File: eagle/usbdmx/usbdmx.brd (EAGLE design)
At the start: 63.2 x 50.2 mm, 34 parts, among them IC1 MAX3468CSA, IC2 MAX3468CSA, Q1 16MHz

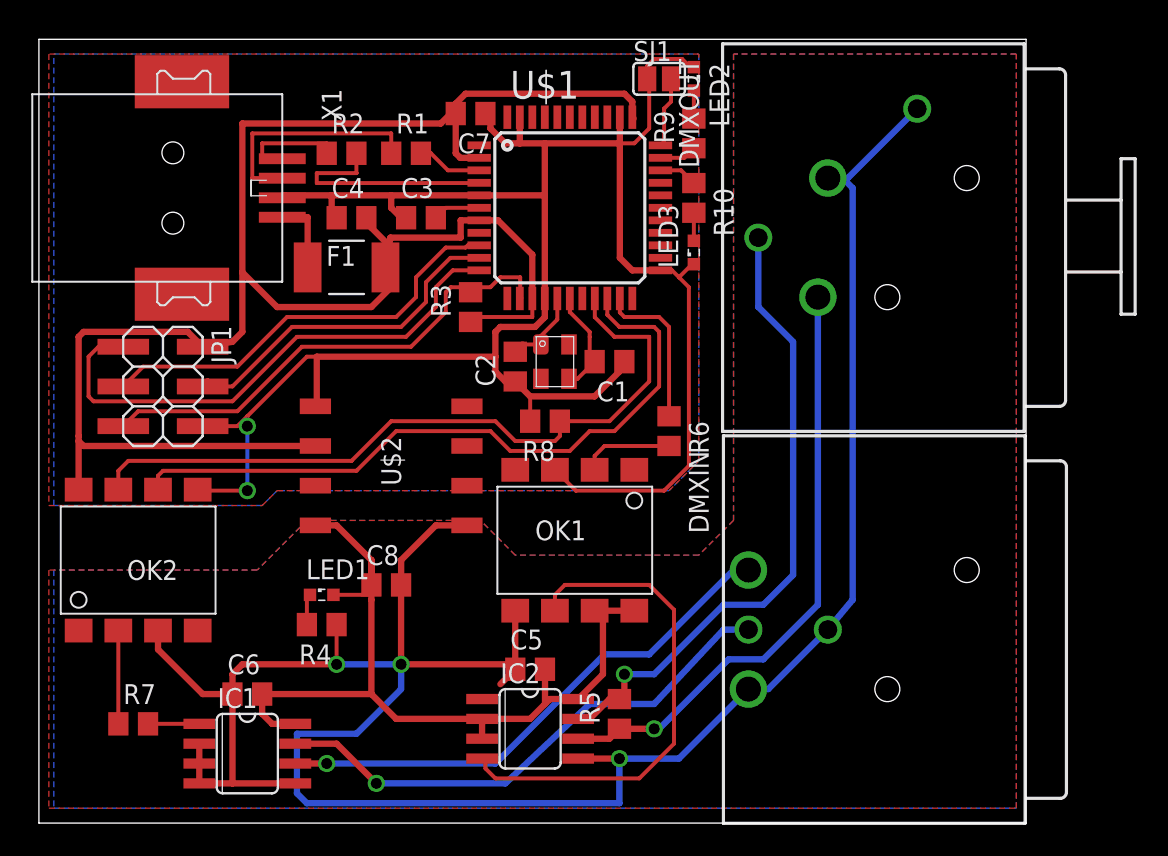
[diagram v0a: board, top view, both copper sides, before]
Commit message: make design smaller since the neutriks can be put closer
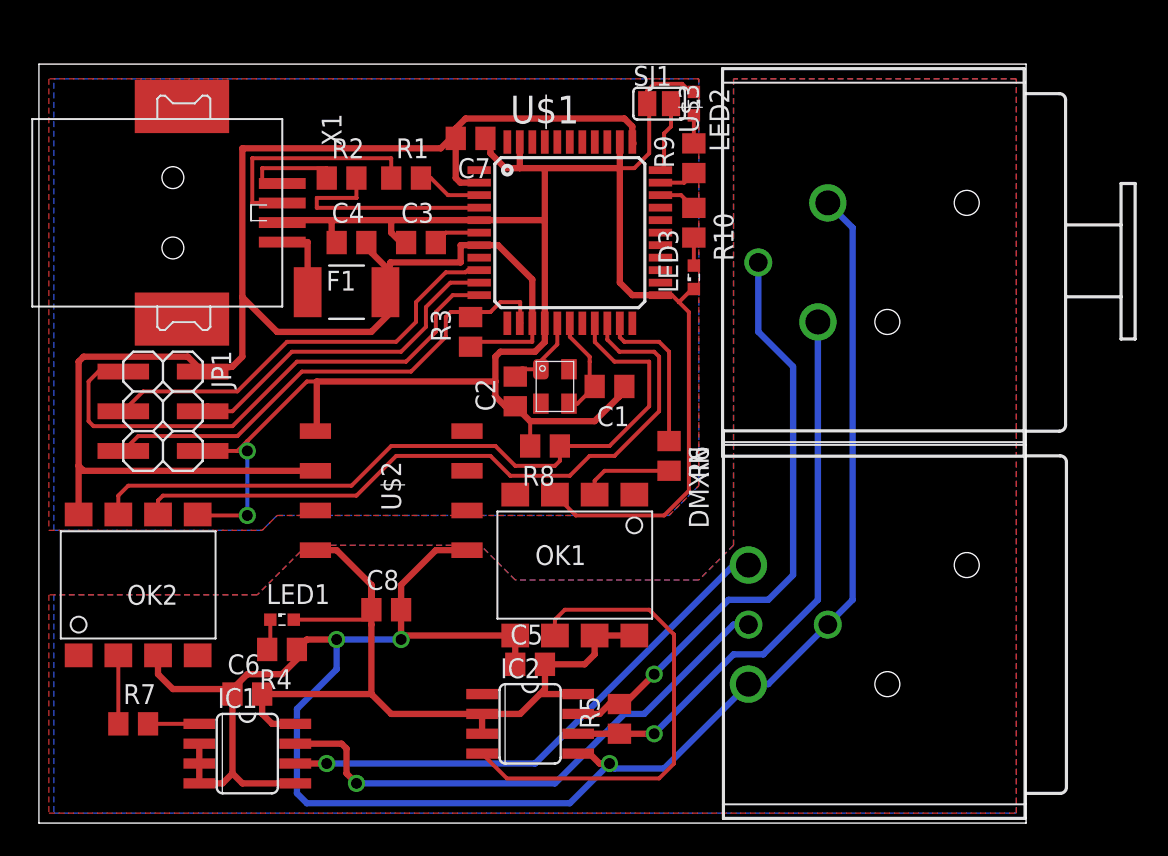
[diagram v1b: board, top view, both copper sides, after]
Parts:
- removed DMXOUT: NC3FAH2, con-neutrik_ag:NC3FAH2
- added U$3: NC3SANSFAH1, con-neutrik_ag:NC3FAH1
- DMXIN: value NC3MBH -> NC3MBH-B; device con-neutrik_ag:NC3MBH -> con-neutrik_ag:NC3MBH-B
- moved LED1 3.00 mm to (15.6, 13.0)
- moved R4 3.00 mm to (15.6, 11.1)
- moved C7 1.59 mm to (27.6, 43.8)
- moved F1 1.59 mm to (19.7, 34.0)
- moved LED3 1.59 mm to (41.9, 34.9)
- moved R10 1.59 mm to (41.9, 38.4)
- moved C2 1.59 mm to (30.5, 27.6)
- moved JP1 1.59 mm to (9.21, 27.6)
- moved R3 1.59 mm to (27.6, 31.4)
- moved R8 1.59 mm to (32.4, 24.1)
- moved C8 1.59 mm to (22.2, 13.7)
- moved OK2 1.59 mm to (6.35, 15.2)
- moved C1 1.59 mm to (36.5, 27.9)
- moved C3 1.59 mm to (24.4, 37.1)
- moved C4 1.59 mm to (20.0, 37.1)
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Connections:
- net N$12: now also U$3.2; no longer DMXOUT.2
- net N$17: now also U$3.3; no longer DMXOUT.3
- net SGND: now also U$3.1+G; no longer DMXOUT.1, DMXOUT.G
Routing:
- net SGND: track 154.5 -> 132.0 mm
- net N$17: track 40.8 -> 38.4 mm
- net SVCC: track 56.5 -> 54.4 mm
- net N$12: track 38.6 -> 36.7 mm
- net N$23: track 5.97 -> 4.38 mm
- net N$29: track 34.1 -> 35.2 mm
- net N$20: track 32.1 -> 31.1 mm
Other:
- board size 63.2 x 50.2 mm -> 63.2 x 48.6 mm

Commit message: add a necessary pull-up
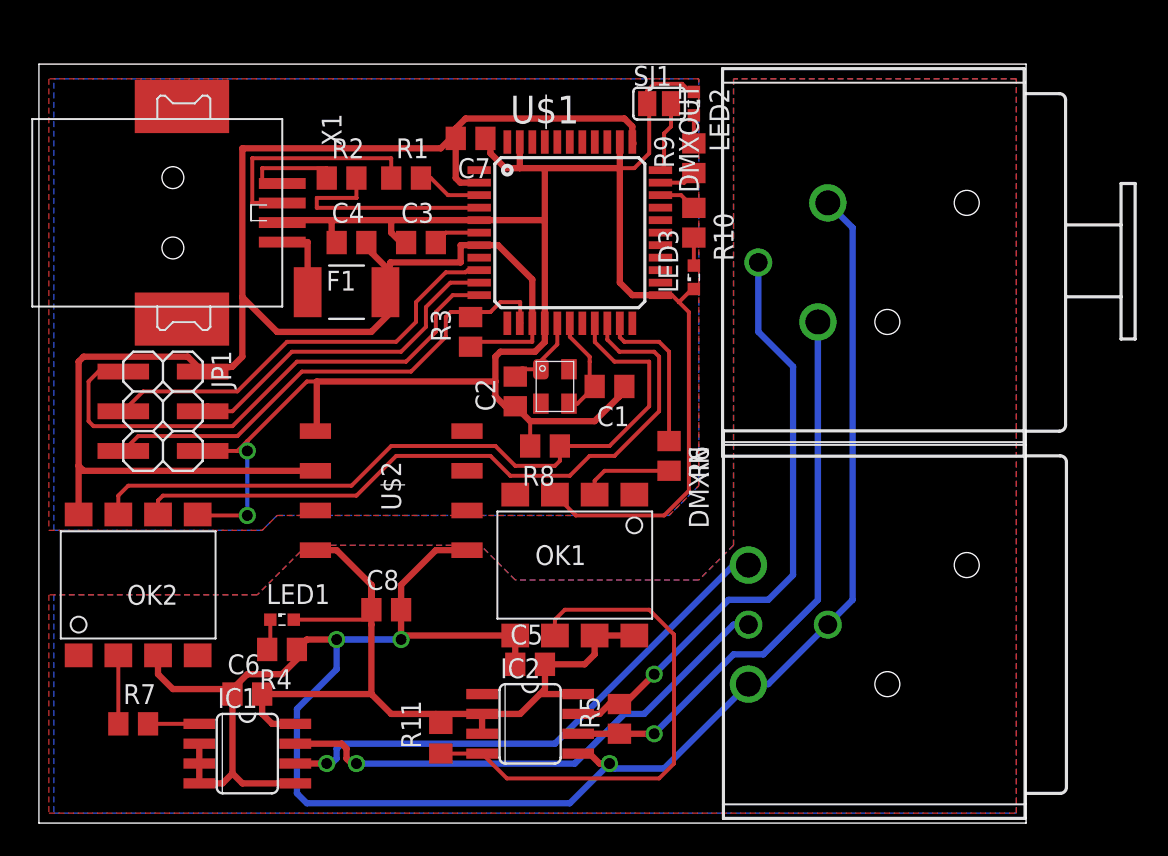
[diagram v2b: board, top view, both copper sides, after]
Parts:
- added R11: 10k, rcl:R0805
- renumbered U$3 to DMXOUT
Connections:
- net N$20: now also R11.1
- net SVCC: now also R11.2
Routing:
- net N$20: track 31.1 -> 33.8 mm
- net N$29: track 35.2 -> 33.6 mm
- net SVCC: track 54.4 -> 55.1 mm
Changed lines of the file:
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@@
 <layer number="23" name="tOrigins" color="15" fill="1" visible="yes" active="yes"/>
 <layer number="24" name="bOrigins" color="15" fill="1" visible="yes" active="yes"/>
-<layer number="25" name="tNames" color="7" fill="1" visible="yes" active="yes"/>
+<layer number="25" name="tNames" color="7" fill="1" visible="no" active="yes"/>
 <layer number="26" name="bNames" color="7" fill="1" visible="yes" active="yes"/>
-<layer number="27" name="tValues" color="7" fill="1" visible="yes" active="yes"/>
+<layer number="27" name="tValues" color="7" fill="1" visible="no" active="yes"/>
 <layer number="28" name="bValues" color="7" fill="1" visible="yes" active="yes"/>
 <layer number="29" name="tStop" color="7" fill="3" visible="no" active="yes"/>
@@
 <element name="LED3" library="led" package="SML0603" value="" x="41.91" y="34.925" rot="R90"/>
 <element name="SJ1" library="jumper" package="SJ" value="" x="39.6875" y="46.0375"/>
-<element name="U$3" library="con-neutrik_ag" package="NC3FAH1" value="NC3SANSFAH1" x="49.8475" y="35.8775" rot="R270"/>
+<element name="DMXOUT" library="con-neutrik_ag" package="NC3FAH1" value="NC3SANSFAH1" x="49.8475" y="35.8775" rot="R270"/>
+<element name="R11" library="rcl" package="R0805" value="10k" x="25.7175" y="5.3975" rot="R90"/>
 </elements>
 <signals>
@@
 <wire x1="48.26" y1="29.21" x2="46.0325" y2="31.4375" width="0.4064" layer="16"/>
 <wire x1="46.6725" y1="14.2875" x2="44.1325" y2="14.2875" width="0.4064" layer="16"/>
-<contactref element="U$3" pad="3"/>
+<contactref element="DMXOUT" pad="3"/>
 <wire x1="46.0325" y1="31.4375" x2="46.0325" y2="35.8775" width="0.4064" layer="16"/>
 <wire x1="34.5059" y1="6.985" x2="35.8775" y2="6.985" width="0.4064" layer="1"/>
@@
 <wire x1="21.2725" y1="15.24" x2="21.2725" y2="15.2425" width="0.4064" layer="1"/>
 <wire x1="21.2725" y1="15.2425" x2="21.275" y2="13.6525" width="0.4064" layer="1"/>
-<contactref element="OK1" pad="8"/>
 <contactref element="OK1" pad="7"/>
 <wire x1="28.3591" y1="6.985" x2="28.3591" y2="5.715" width="0.4064" layer="1"/>
@@
 <wire x1="16.3075" y1="13.0175" x2="21.275" y2="13.0175" width="0.254" layer="1"/>
 <wire x1="21.275" y1="13.0175" x2="21.275" y2="12.7" width="0.254" layer="1"/>
-<wire x1="38.1" y1="12.0015" x2="36.195" y2="12.0015" width="0.4064" layer="1"/>
 <wire x1="36.195" y1="12.0015" x2="35.56" y2="12.0015" width="0.4064" layer="1"/>
 <wire x1="35.875" y1="11.6865" x2="35.56" y2="12.0015" width="0.4064" layer="1"/>
@@
 <wire x1="14.2875" y1="6.985" x2="14.2875" y2="8.2525" width="0.4064" layer="1"/>
 <wire x1="14.2875" y1="8.2525" x2="14.285" y2="8.255" width="0.4064" layer="1"/>
-<wire x1="28.3591" y1="6.985" x2="22.545" y2="6.985" width="0.4064" layer="1"/>
+<wire x1="28.3591" y1="6.985" x2="25.4" y2="6.985" width="0.4064" layer="1"/>
+<wire x1="25.4" y1="6.985" x2="22.545" y2="6.985" width="0.4064" layer="1"/>
 <wire x1="22.545" y1="6.985" x2="21.275" y2="8.255" width="0.4064" layer="1"/>
+<contactref element="OK1" pad="8"/>
+<contactref element="R11" pad="2"/>
+<wire x1="25.7175" y1="6.3475" x2="25.4" y2="6.665" width="0.254" layer="1"/>
+<wire x1="25.4" y1="6.665" x2="25.4" y2="6.985" width="0.254" layer="1"/>
+<wire x1="36.195" y1="12.0015" x2="38.1" y2="12.0015" width="0.4064" layer="1"/>
 </signal>
 <signal name="SGND">
@@
 <wire x1="16.51" y1="7.3025" x2="16.51" y2="1.905" width="0.4064" layer="16"/>
 <wire x1="16.51" y1="1.905" x2="17.145" y2="1.27" width="0.4064" layer="16"/>
-<contactref element="U$3" pad="1+G"/>
+<contactref element="DMXOUT" pad="1+G"/>
 <wire x1="52.07" y1="14.2875" x2="52.07" y2="38.1" width="0.4064" layer="16"/>
 <wire x1="52.07" y1="38.1" x2="50.4825" y2="39.6875" width="0.4064" layer="16"/>
@@
 <wire x1="39.6875" y1="2.8575" x2="40.64" y2="3.81" width="0.254" layer="1"/>
 <wire x1="40.64" y1="3.81" x2="40.64" y2="12.065" width="0.254" layer="1"/>
+<contactref element="R11" pad="1"/>
+<wire x1="28.3591" y1="4.445" x2="28.3566" y2="4.4475" width="0.254" layer="1"/>
+<wire x1="28.3566" y1="4.4475" x2="25.7175" y2="4.4475" width="0.254" layer="1"/>
 </signal>
 <signal name="N$21">
@@
 <contactref element="IC2" pad="6"/>
 <contactref element="R5" pad="1"/>
-<contactref element="U$3" pad="2"/>
+<contactref element="DMXOUT" pad="2"/>
 <wire x1="49.8475" y1="14.2875" x2="49.8475" y2="32.0675" width="0.4064" layer="16"/>
 <wire x1="34.5059" y1="5.715" x2="37.145" y2="5.715" width="0.4064" layer="1"/>
@@
 <contactref element="IC1" pad="7"/>
 <contactref element="DMXIN" pad="3"/>
-<via x="20.32" y="2.54" extent="1-16" drill="0.7" shape="square"/>
-<wire x1="20.32" y1="2.54" x2="33.02" y2="2.54" width="0.4064" layer="16"/>
+<via x="20.32" y="3.81" extent="1-16" drill="0.7" shape="square"/>
+<wire x1="20.32" y1="3.81" x2="34.29" y2="3.81" width="0.4064" layer="16"/>
 <wire x1="16.4084" y1="5.08" x2="19.3675" y2="5.08" width="0.4064" layer="1"/>
-<wire x1="19.3675" y1="5.08" x2="19.685" y2="4.7625" width="0.4064" layer="1"/>
-<wire x1="19.685" y1="4.7625" x2="19.685" y2="3.175" width="0.4064" layer="1"/>
-<wire x1="19.685" y1="3.175" x2="20.32" y2="2.54" width="0.4064" layer="1"/>
-<wire x1="33.02" y1="2.54" x2="37.465" y2="6.985" width="0.4064" layer="16"/>
+<wire x1="34.29" y1="3.81" x2="37.465" y2="6.985" width="0.4064" layer="16"/>
 <wire x1="37.465" y1="6.985" x2="38.735" y2="6.985" width="0.4064" layer="16"/>
 <wire x1="38.735" y1="6.985" x2="44.45" y2="12.7" width="0.4064" layer="16"/>
 <wire x1="44.45" y1="12.7" x2="45.4025" y2="12.7" width="0.4064" layer="16"/>
+<wire x1="19.3675" y1="5.08" x2="19.685" y2="4.7625" width="0.4064" layer="1"/>
+<wire x1="19.685" y1="4.7625" x2="19.685" y2="4.1275" width="0.4064" layer="1"/>
+<wire x1="19.685" y1="4.1275" x2="20.0025" y2="3.81" width="0.4064" layer="1"/>
+<wire x1="20.0025" y1="3.81" x2="20.32" y2="3.81" width="0.4064" layer="1"/>
 </signal>
 <signal name="N$18">
@@
 <contactref element="IC1" pad="6"/>
 <via x="18.415" y="3.81" extent="1-16" drill="0.7" shape="square"/>
-<wire x1="18.415" y1="3.81" x2="31.75" y2="3.81" width="0.4064" layer="16"/>
 <wire x1="16.4084" y1="3.81" x2="18.415" y2="3.81" width="0.4064" layer="1"/>
-<wire x1="31.75" y1="3.81" x2="44.45" y2="16.51" width="0.4064" layer="16"/>
 <wire x1="44.45" y1="16.51" x2="45.4025" y2="16.51" width="0.4064" layer="16"/>
+<wire x1="33.02" y1="5.08" x2="44.45" y2="16.51" width="0.4064" layer="16"/>
+<wire x1="18.415" y1="3.81" x2="18.7325" y2="3.81" width="0.4064" layer="16"/>
+<wire x1="18.7325" y1="3.81" x2="19.05" y2="4.1275" width="0.4064" layer="16"/>
+<wire x1="19.05" y1="4.1275" x2="19.05" y2="4.7625" width="0.4064" layer="16"/>
+<wire x1="19.05" y1="4.7625" x2="19.3675" y2="5.08" width="0.4064" layer="16"/>
+<wire x1="19.3675" y1="5.08" x2="33.02" y2="5.08" width="0.4064" layer="16"/>
 </signal>
 <signal name="N$19">

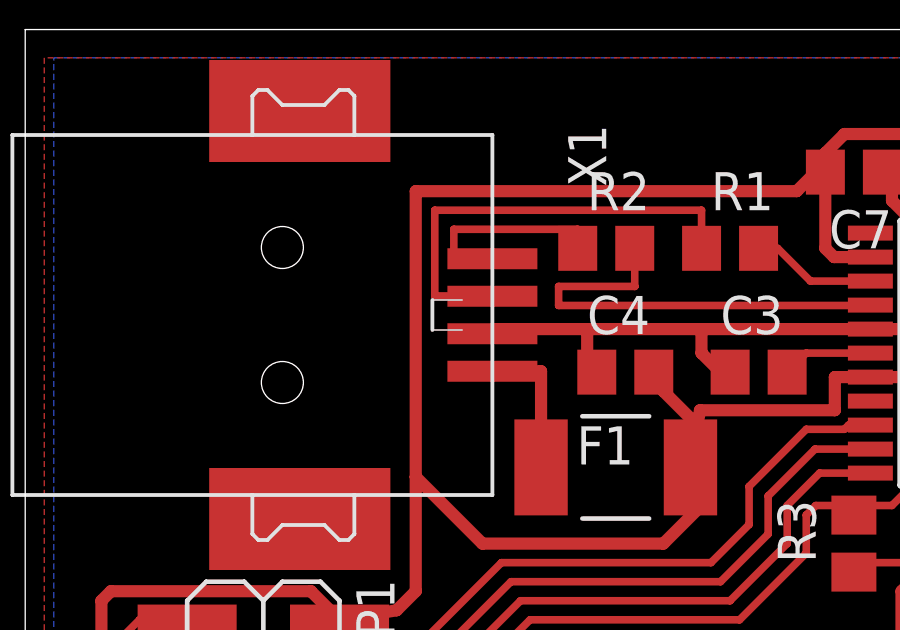
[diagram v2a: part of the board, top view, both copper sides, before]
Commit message: fix usb port drill holes
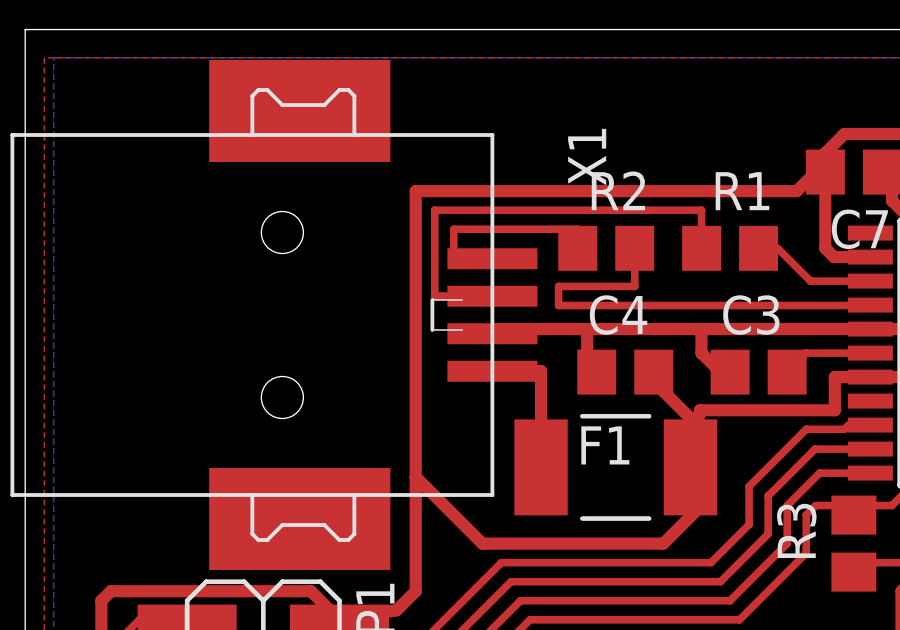
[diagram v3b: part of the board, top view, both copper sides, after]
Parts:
- X1: device con-usb-3:USB-B-SMT -> con-usb-3:USB-B-SMT-R
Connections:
- net GND: now also X1.5, X1.6
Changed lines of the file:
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@@
 <element name="R3" library="rcl" package="R0805" value="10k" x="27.6225" y="31.4325" rot="R90"/>
 <element name="U$1" library="adafruit" package="TQFP44" value="ATMEGA32U4-AU" x="33.9725" y="37.7825"/>
-<element name="X1" library="con-usb-3" package="USB-B-SMT" value="" x="8.5725" y="39.0525"/>
+<element name="X1" library="con-usb-3" package="USB-B-SMT-R" value="" x="8.5725" y="39.0525"/>
 <element name="C4" library="rcl" package="C0805" value="100n" x="20.0025" y="37.1475"/>
 <element name="C5" library="rcl" package="C0805" value="100n" x="31.4325" y="10.16"/>
@@
 <wire x1="39.0525" y1="45.9105" x2="39.0525" y2="42.8625" width="0.254" layer="1"/>
 <wire x1="39.0525" y1="42.8625" x2="38.1" y2="41.91" width="0.254" layer="1"/>
+<contactref element="X1" pad="5"/>
+<contactref element="X1" pad="6"/>
 </signal>
 <signal name="N$2">
@@
 <wire x1="17.78" y1="39.37" x2="28.1725" y2="39.37" width="0.254" layer="1"/>
 <wire x1="28.1725" y1="39.37" x2="28.1725" y2="39.3825" width="0.4064" layer="1"/>
-<wire x1="17.78" y1="40.005" x2="20.32" y2="40.005" width="0.254" layer="1"/>
-<wire x1="20.32" y1="40.005" x2="20.3175" y2="40.0075" width="0.254" layer="1"/>
-<wire x1="20.3175" y1="40.0075" x2="20.3175" y2="41.275" width="0.254" layer="1"/>
+<wire x1="20.3175" y1="41.275" x2="20.3175" y2="40.005" width="0.254" layer="1"/>
+<wire x1="20.3175" y1="40.005" x2="17.78" y2="40.005" width="0.254" layer="1"/>
 </signal>
 <signal name="N$5">
